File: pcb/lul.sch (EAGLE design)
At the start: 87 parts, among them IC1 STM32F072C8T6, IC2 REG1117, IC3 74AHCT1G08DBV, SW1 324_SW324_SWITCH_FOOT_HOLE, SW2 324_SW324_SWITCH_FOOT_HOLE, U1 UG-2864HSWEG01

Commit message: new buttons
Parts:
- removed S19, S20: TAC_SWITCHSMD, clock:TAC_SWITCHSMD
- removed U$12, U$13: M3_MOUNTING_HOLE, clock:M3_MOUNTING_HOLE
- added SW3, SW4: 6X6_SW, lul:6X6_SW
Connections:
- net BUTTON1: now also IC1PORTA_L.PA1, SW3.1; no longer IC1PORTB_H.PB12, S19.1, S19.2
- net BUTTON2: now also IC1PORTA_L.PA2, SW4.1; no longer IC1PORTB_H.PB11, S20.1, S20.2
- net GND: now also SW3.2, SW4.2; no longer S19.3, S19.4, S20.3, S20.4
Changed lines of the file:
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@@
 <part name="SD1" library="clock" deviceset="TF-HOLDER" device=""/>
 <part name="JP1" library="pinhead" library_urn="urn:adsk.eagle:library:325" deviceset="PINHD-1X5" device=""/>
-<part name="S19" library="clock" deviceset="TAC_SWITCH" device="SMD" value="TAC_SWITCHSMD"/>
-<part name="S20" library="clock" deviceset="TAC_SWITCH" device="SMD" value="TAC_SWITCHSMD"/>
 <part name="IC2" library="clock" deviceset="REG1117" device=""/>
 <part name="+3V3" library="supply1" library_urn="urn:adsk.eagle:library:371" deviceset="+3V3" device=""/>
@@
 <part name="U$10" library="clock" deviceset="M3_MOUNTING_HOLE" device=""/>
 <part name="U$11" library="clock" deviceset="M3_MOUNTING_HOLE" device=""/>
-<part name="U$12" library="clock" deviceset="M3_MOUNTING_HOLE" device=""/>
-<part name="U$13" library="clock" deviceset="M3_MOUNTING_HOLE" device=""/>
 <part name="U$14" library="clock" deviceset="M3_MOUNTING_HOLE" device=""/>
 <part name="U$15" library="clock" deviceset="M3_MOUNTING_HOLE" device=""/>
@@
 <part name="SW1" library="3pos_slide_switch" deviceset="324_SW" device="324_SWITCH_FOOT_HOLE" value="324_SW324_SWITCH_FOOT_HOLE"/>
 <part name="C28" library="clock" deviceset="CAP" device="0805" value="1uF"/>
+<part name="SW3" library="lul" deviceset="6X6_SW" device=""/>
+<part name="SW4" library="lul" deviceset="6X6_SW" device=""/>
 </parts>
 <sheets>
@@
 <instance part="SD1" gate="G$1" x="320.04" y="-162.56" rot="MR0"/>
 <instance part="JP1" gate="A" x="358.14" y="-193.04" rot="R180"/>
-<instance part="S19" gate="S" x="144.78" y="-170.18"/>
-<instance part="S20" gate="S" x="144.78" y="-193.04"/>
 <instance part="IC2" gate="G$1" x="109.22" y="-144.78"/>
 <instance part="+3V3" gate="G$1" x="353.06" y="76.2"/>
@@
 <instance part="+3V7" gate="G$1" x="259.08" y="-180.34" rot="MR0"/>
 <instance part="GND10" gate="1" x="254" y="-175.26"/>
-<instance part="GND11" gate="1" x="157.48" y="-175.26"/>
+<instance part="GND11" gate="1" x="172.72" y="-175.26"/>
 <instance part="+3V8" gate="G$1" x="294.64" y="-86.36"/>
 <instance part="GND12" gate="1" x="294.64" y="-121.92"/>
@@
 <instance part="R17" gate="G$1" x="408.94" y="-165.1" rot="R90"/>
 <instance part="GND45" gate="1" x="408.94" y="-175.26"/>
-<instance part="GND19" gate="1" x="154.94" y="-198.12"/>
+<instance part="GND19" gate="1" x="175.26" y="-198.12"/>
 <instance part="LED1" gate="G$1" x="-185.42" y="25.4" rot="MR0"/>
 <instance part="GND1" gate="1" x="139.7" y="-68.58"/>
@@
 <instance part="U$10" gate="G$1" x="467.36" y="33.02"/>
 <instance part="U$11" gate="G$1" x="523.24" y="33.02"/>
-<instance part="U$12" gate="G$1" x="523.24" y="15.24"/>
-<instance part="U$13" gate="G$1" x="495.3" y="33.02"/>
 <instance part="U$14" gate="G$1" x="467.36" y="15.24"/>
 <instance part="U$15" gate="G$1" x="495.3" y="48.26"/>
@@
 <instance part="SW1" gate="G$1" x="243.84" y="-205.74" rot="MR270"/>
 <instance part="C28" gate="G$1" x="335.28" y="-2.54" rot="R90"/>
+<instance part="SW3" gate="G$1" x="154.94" y="-172.72"/>
+<instance part="SW4" gate="G$1" x="152.4" y="-195.58"/>
 </instances>
 <busses>
@@
 <pinref part="U$3" gate="1" pin="GND"/>
 <junction x="297.18" y="-30.48"/>
-</segment>
-<segment>
-<pinref part="S19" gate="S" pin="4"/>
-<wire x1="149.86" y1="-172.72" x2="157.48" y2="-172.72" width="0.1524" layer="91"/>
-<pinref part="GND11" gate="1" pin="GND"/>
-<pinref part="S19" gate="S" pin="3"/>
-<wire x1="149.86" y1="-170.18" x2="149.86" y2="-172.72" width="0.1524" layer="91"/>
-<junction x="149.86" y="-172.72"/>
-</segment>
-<segment>
-<pinref part="S20" gate="S" pin="3"/>
-<pinref part="S20" gate="S" pin="4"/>
-<wire x1="149.86" y1="-193.04" x2="149.86" y2="-195.58" width="0.1524" layer="91"/>
-<pinref part="GND19" gate="1" pin="GND"/>
-<wire x1="149.86" y1="-195.58" x2="154.94" y2="-195.58" width="0.1524" layer="91"/>
-<junction x="149.86" y="-195.58"/>
 </segment>
 <segment>
@@
 <junction x="246.38" y="-172.72"/>
 </segment>
+<segment>
+<pinref part="GND11" gate="1" pin="GND"/>
+<pinref part="SW3" gate="G$1" pin="2"/>
+<wire x1="167.64" y1="-172.72" x2="172.72" y2="-172.72" width="0.1524" layer="91"/>
+</segment>
+<segment>
+<pinref part="GND19" gate="1" pin="GND"/>
+<pinref part="SW4" gate="G$1" pin="2"/>
+<wire x1="165.1" y1="-195.58" x2="175.26" y2="-195.58" width="0.1524" layer="91"/>
+</segment>
 </net>
 <net name="SCL" class="0">
@@
 <net name="BUTTON1" class="0">
 <segment>
-<pinref part="S19" gate="S" pin="2"/>
-<wire x1="127" y1="-172.72" x2="139.7" y2="-172.72" width="0.1524" layer="91"/>
-<pinref part="S19" gate="S" pin="1"/>
-<wire x1="139.7" y1="-170.18" x2="139.7" y2="-172.72" width="0.1524" layer="91"/>
-<junction x="139.7" y="-172.72"/>
+<wire x1="127" y1="-172.72" x2="142.24" y2="-172.72" width="0.1524" layer="91"/>
 <label x="127" y="-172.72" size="1.778" layer="95"/>
-</segment>
-<segment>
-<pinref part="IC1" gate="PORTB_H" pin="PB12"/>
-<wire x1="449.58" y1="-193.04" x2="434.34" y2="-193.04" width="0.1524" layer="91"/>
-<label x="439.42" y="-193.04" size="1.778" layer="95"/>
+<pinref part="SW3" gate="G$1" pin="1"/>
+</segment>
+<segment>
+<pinref part="IC1" gate="PORTA_L" pin="PA1"/>
+<wire x1="363.22" y1="-157.48" x2="391.16" y2="-157.48" width="0.1524" layer="91"/>
+<label x="365.76" y="-157.48" size="1.778" layer="95"/>
 </segment>
 </net>
 <net name="BUTTON2" class="0">
 <segment>
-<pinref part="S20" gate="S" pin="2"/>
 <wire x1="124.46" y1="-195.58" x2="139.7" y2="-195.58" width="0.1524" layer="91"/>
-<pinref part="S20" gate="S" pin="1"/>
-<wire x1="139.7" y1="-193.04" x2="139.7" y2="-195.58" width="0.1524" layer="91"/>
-<junction x="139.7" y="-195.58"/>
 <label x="124.46" y="-195.58" size="1.778" layer="95"/>
-</segment>
-<segment>
-<pinref part="IC1" gate="PORTB_H" pin="PB11"/>
-<wire x1="449.58" y1="-190.5" x2="434.34" y2="-190.5" width="0.1524" layer="91"/>
-<label x="439.42" y="-190.5" size="1.778" layer="95"/>
-</segment>
-</net>
+<pinref part="SW4" gate="G$1" pin="1"/>
+</segment>
+<segment>
+<pinref part="IC1" gate="PORTA_L" pin="PA2"/>
+<wire x1="363.22" y1="-160.02" x2="391.16" y2="-160.02" width="0.1524" layer="91"/>
+<label x="365.76" y="-160.02" size="1.778" layer="95"/>
+</segment>
+</net>

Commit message: clean up main folder
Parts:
- C1, C10, C11, C12, C13, C14, C15, C16, C17, C18, C19, C2, C20, C21, C22, C23, C24, C25, C9: value 0.1uF -> 100nF
- C8: value 2.2uF/16V -> 2.2uF
- R2, R4, R5: value 10k -> 10K
- R7, R8: value 4K7 -> 5.1K
- S1, S10, S11, S12, S13, S14, S15, S2, S3, S4, S5, S6, S7, S8, S9: value MOMENTARY-SWITCH-SPST-LED-PTH-CHERRY -> CHERRY-MX-LED; device lul:MOMENTARY-SWITCH-SPST-LED-PTH-CHERRY -> SparkFun-Cherry-MX-Switch-Breakout:CHERRY-MX-LED
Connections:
- net GND: now also S1.S2, S10.S2, S11.S2, S12.S2, S13.S2, S14.S2, S15.S2, S2.S2, S3.S2, S4.S2, S5.S2, S6.S2, S7.S2, S8.S2, S9.S2; no longer S1.2, S10.2, S11.2, S12.2, S13.2, S14.2, S15.2, S2.2, S3.2, S4.2, S5.2, S6.2, S7.2, S8.2, S9.2
- net SW1: now also S1.S1; no longer S1.1
- net SW10: now also S10.S1; no longer S10.1
- net SW11: now also S11.S1; no longer S11.1
- net SW12: now also S12.S1; no longer S12.1
- net SW13: now also S13.S1; no longer S13.1
- net SW14: now also S14.S1; no longer S14.1
- net SW15: now also S15.S1; no longer S15.1
- net SW2: now also S2.S1; no longer S2.1
- net SW3: now also S3.S1; no longer S3.1
- net SW4: now also S4.S1; no longer S4.1
- net SW5: now also S5.S1; no longer S5.1
- net SW6: now also S6.S1; no longer S6.1
- net SW7: now also S7.S1; no longer S7.1
- net SW8: now also S8.S1; no longer S8.1
- net SW9: now also S9.S1; no longer S9.1

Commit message: new pcb ready for fab
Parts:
- removed C26: 47uF, clock:C-USC1210
- added C29: 100nF, clock:CAP0805
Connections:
- net GND: now also C29.1; no longer C26.2
- net N$1: now also C29.2; no longer C26.1
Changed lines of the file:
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@@
 <part name="R1" library="joyAnalog" deviceset="RESISTOR" device="0805-RES" value="5.1K"/>
 <part name="R9" library="joyAnalog" deviceset="RESISTOR" device="0805-RES" value="5.1K"/>
-<part name="C26" library="clock" deviceset="C-US" device="C1210" value="47uF"/>
-<part name="GND5" library="supply1" library_urn="urn:adsk.eagle:library:371" deviceset="GND" device=""/>
 <part name="GND8" library="supply1" library_urn="urn:adsk.eagle:library:371" deviceset="GND" device=""/>
 <part name="SW2" library="3pos_slide_switch" deviceset="324_SW" device="324_SWITCH_FOOT_HOLE" value="324_SW324_SWITCH_FOOT_HOLE"/>
@@
 <part name="SW3" library="lul" deviceset="6X6_SW" device=""/>
 <part name="SW4" library="lul" deviceset="6X6_SW" device=""/>
+<part name="C29" library="clock" deviceset="CAP" device="0805" value="100nF"/>
+<part name="GND16" library="supply1" library_urn="urn:adsk.eagle:library:371" deviceset="GND" device=""/>
 </parts>
 <sheets>
@@
 <instance part="R1" gate="G$1" x="-5.08" y="-154.94" rot="MR0"/>
 <instance part="R9" gate="G$1" x="-5.08" y="-149.86" rot="MR0"/>
-<instance part="C26" gate="G$1" x="86.36" y="-147.32"/>
-<instance part="GND5" gate="1" x="86.36" y="-154.94"/>
 <instance part="GND8" gate="1" x="276.86" y="-213.36"/>
 <instance part="SW2" gate="G$1" x="241.3" y="-157.48" rot="MR90"/>
@@
 <instance part="SW3" gate="G$1" x="154.94" y="-172.72"/>
 <instance part="SW4" gate="G$1" x="152.4" y="-195.58"/>
+<instance part="C29" gate="G$1" x="78.74" y="-147.32" rot="R180"/>
+<instance part="GND16" gate="1" x="78.74" y="-154.94"/>
 </instances>
 <busses>
@@
 </segment>
 <segment>
-<pinref part="C26" gate="G$1" pin="2"/>
-<pinref part="GND5" gate="1" pin="GND"/>
-</segment>
-<segment>
 <pinref part="SW2" gate="G$1" pin="2"/>
 <pinref part="GND10" gate="1" pin="GND"/>
@@
 <pinref part="SW4" gate="G$1" pin="2"/>
 <wire x1="165.1" y1="-195.58" x2="175.26" y2="-195.58" width="0.1524" layer="91"/>
+</segment>
+<segment>
+<pinref part="C29" gate="G$1" pin="1"/>
+<pinref part="GND16" gate="1" pin="GND"/>
 </segment>
 </net>
@@
 <pinref part="U$8" gate="G$1" pin="VBUS"/>
 <pinref part="IC2" gate="G$1" pin="VIN"/>
-<wire x1="43.18" y1="-144.78" x2="86.36" y2="-144.78" width="0.1524" layer="91"/>
-<pinref part="C26" gate="G$1" pin="1"/>
-<wire x1="86.36" y1="-144.78" x2="96.52" y2="-144.78" width="0.1524" layer="91"/>
-<junction x="86.36" y="-144.78"/>
-</segment>
-</net>
+<wire x1="43.18" y1="-144.78" x2="78.74" y2="-144.78" width="0.1524" layer="91"/>
+<wire x1="78.74" y1="-144.78" x2="96.52" y2="-144.78" width="0.1524" layer="91"/>
+<pinref part="C29" gate="G$1" pin="2"/>
+<junction x="78.74" y="-144.78"/>
+</segment>
+</net>

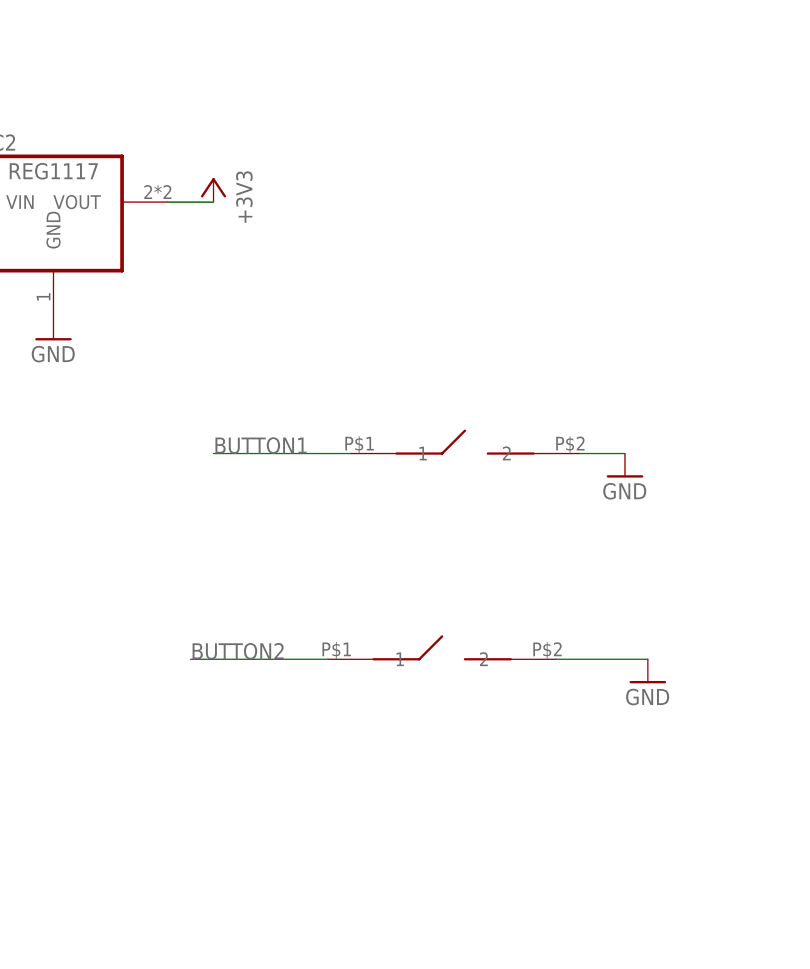
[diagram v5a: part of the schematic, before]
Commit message: firmware improvment, new plus/minus buttons
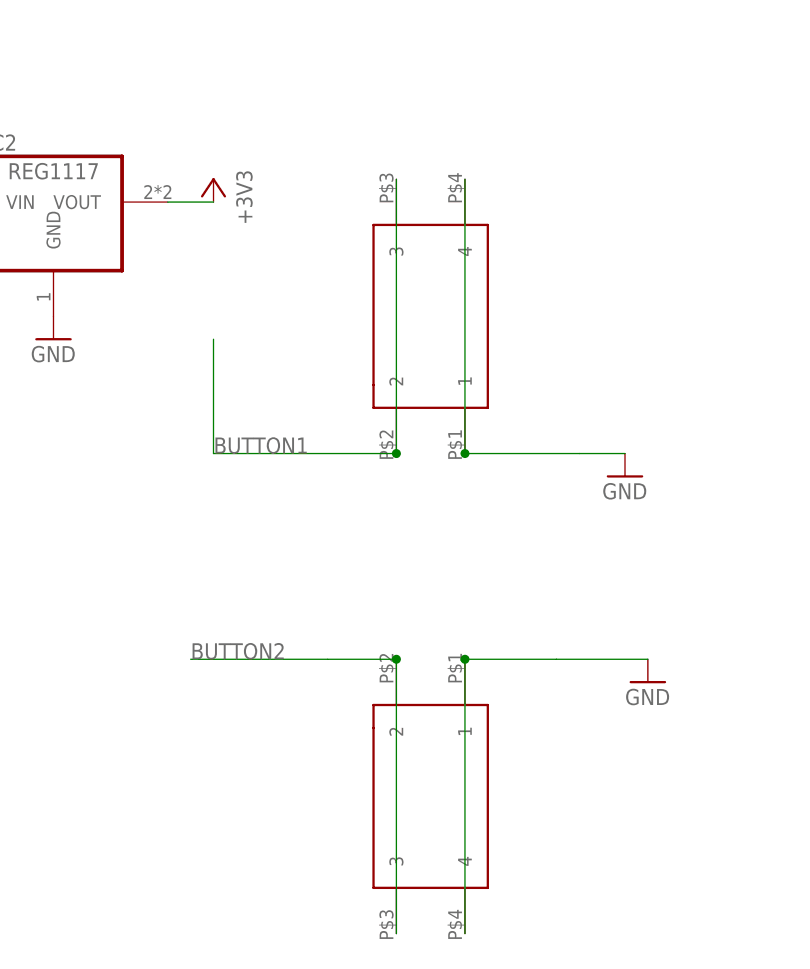
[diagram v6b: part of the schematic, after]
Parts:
- SW3, SW4: value 6X6_SW -> 324_SW324_SWITCH_FOOT_HOLE; device lul:6X6_SW -> 3pos_slide_switch:324_SW324_SWITCH_FOOT_HOLE
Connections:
- net BUTTON1: now also SW3.2, SW3.3; no longer SW3.1
- net BUTTON2: now also SW4.2, SW4.3; no longer SW4.1
- net GND: now also SW3.1, SW3.4, SW4.1, SW4.4; no longer SW3.2, SW4.2
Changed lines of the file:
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@@
 <part name="SW1" library="3pos_slide_switch" deviceset="324_SW" device="324_SWITCH_FOOT_HOLE" value="324_SW324_SWITCH_FOOT_HOLE"/>
 <part name="C28" library="clock" deviceset="CAP" device="0805" value="1uF"/>
-<part name="SW3" library="lul" deviceset="6X6_SW" device=""/>
-<part name="SW4" library="lul" deviceset="6X6_SW" device=""/>
 <part name="C29" library="clock" deviceset="CAP" device="0805" value="100nF"/>
 <part name="GND16" library="supply1" library_urn="urn:adsk.eagle:library:371" deviceset="GND" device=""/>
+<part name="SW3" library="3pos_slide_switch" deviceset="324_SW" device="324_SWITCH_FOOT_HOLE" value="324_SW324_SWITCH_FOOT_HOLE"/>
+<part name="SW4" library="3pos_slide_switch" deviceset="324_SW" device="324_SWITCH_FOOT_HOLE" value="324_SW324_SWITCH_FOOT_HOLE"/>
 </parts>
 <sheets>
@@
 <instance part="SW1" gate="G$1" x="243.84" y="-205.74" rot="MR270"/>
 <instance part="C28" gate="G$1" x="335.28" y="-2.54" rot="R90"/>
-<instance part="SW3" gate="G$1" x="154.94" y="-172.72"/>
-<instance part="SW4" gate="G$1" x="152.4" y="-195.58"/>
 <instance part="C29" gate="G$1" x="78.74" y="-147.32" rot="R180"/>
 <instance part="GND16" gate="1" x="78.74" y="-154.94"/>
+<instance part="SW3" gate="G$1" x="152.4" y="-157.48" rot="R90"/>
+<instance part="SW4" gate="G$1" x="152.4" y="-210.82" rot="MR270"/>
 </instances>
 <busses>
@@
 <segment>
 <pinref part="GND11" gate="1" pin="GND"/>
-<pinref part="SW3" gate="G$1" pin="2"/>
 <wire x1="167.64" y1="-172.72" x2="172.72" y2="-172.72" width="0.1524" layer="91"/>
+<pinref part="SW3" gate="G$1" pin="1"/>
+<wire x1="154.94" y1="-172.72" x2="167.64" y2="-172.72" width="0.1524" layer="91"/>
+<pinref part="SW3" gate="G$1" pin="4"/>
+<wire x1="154.94" y1="-142.24" x2="154.94" y2="-172.72" width="0.1524" layer="91"/>
+<junction x="154.94" y="-172.72"/>
 </segment>
 <segment>
 <pinref part="GND19" gate="1" pin="GND"/>
-<pinref part="SW4" gate="G$1" pin="2"/>
 <wire x1="165.1" y1="-195.58" x2="175.26" y2="-195.58" width="0.1524" layer="91"/>
+<pinref part="SW4" gate="G$1" pin="1"/>
+<wire x1="154.94" y1="-195.58" x2="165.1" y2="-195.58" width="0.1524" layer="91"/>
+<pinref part="SW4" gate="G$1" pin="4"/>
+<wire x1="154.94" y1="-195.58" x2="154.94" y2="-226.06" width="0.1524" layer="91"/>
+<junction x="154.94" y="-195.58"/>
 </segment>
 <segment>
@@
 <net name="BUTTON1" class="0">
 <segment>
-<wire x1="127" y1="-172.72" x2="142.24" y2="-172.72" width="0.1524" layer="91"/>
 <label x="127" y="-172.72" size="1.778" layer="95"/>
-<pinref part="SW3" gate="G$1" pin="1"/>
+<wire x1="127" y1="-160.02" x2="127" y2="-172.72" width="0.1524" layer="91"/>
+<pinref part="SW3" gate="G$1" pin="2"/>
+<wire x1="127" y1="-172.72" x2="147.32" y2="-172.72" width="0.1524" layer="91"/>
+<pinref part="SW3" gate="G$1" pin="3"/>
+<wire x1="147.32" y1="-142.24" x2="147.32" y2="-172.72" width="0.1524" layer="91"/>
+<junction x="147.32" y="-172.72"/>
 </segment>
 <segment>
@@
 <wire x1="124.46" y1="-195.58" x2="139.7" y2="-195.58" width="0.1524" layer="91"/>
 <label x="124.46" y="-195.58" size="1.778" layer="95"/>
-<pinref part="SW4" gate="G$1" pin="1"/>
-</segment>
-<segment>
+<pinref part="SW4" gate="G$1" pin="2"/>
+<wire x1="139.7" y1="-195.58" x2="147.32" y2="-195.58" width="0.1524" layer="91"/>
+<pinref part="SW4" gate="G$1" pin="3"/>
+<wire x1="147.32" y1="-195.58" x2="147.32" y2="-226.06" width="0.1524" layer="91"/>
+<junction x="147.32" y="-195.58"/>
+</segment>
+<segment>

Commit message: production run 1
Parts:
- renumbered U$8 to U2
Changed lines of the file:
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@@
 <part name="IC3" library="74xx-little-de" library_urn="urn:adsk.eagle:library:86" deviceset="74*1G08" device="DBV" technology="AHCT"/>
 <part name="GND31" library="supply1" library_urn="urn:adsk.eagle:library:371" deviceset="GND" device=""/>
-<part name="U$8" library="my_usbc_16p" deviceset="USBC_16P" device=""/>
+<part name="U2" library="my_usbc_16p" deviceset="USBC_16P" device=""/>
 <part name="GND6" library="supply1" deviceset="GND" device=""/>
 <part name="R1" library="joyAnalog" deviceset="RESISTOR" device="0805-RES" value="5.1K"/>
@@
 <instance part="IC3" gate="P" x="-63.5" y="50.8"/>
 <instance part="GND31" gate="1" x="-45.72" y="7.62"/>
-<instance part="U$8" gate="G$1" x="27.94" y="-165.1" rot="MR0"/>
+<instance part="U2" gate="G$1" x="27.94" y="-165.1" rot="MR0"/>
 <instance part="GND6" gate="1" x="-10.16" y="-172.72" rot="MR0"/>
 <instance part="R1" gate="G$1" x="-5.08" y="-154.94" rot="MR0"/>
@@
 <pinref part="R9" gate="G$1" pin="2"/>
 <wire x1="-10.16" y1="-149.86" x2="-10.16" y2="-154.94" width="0.1524" layer="91"/>
-<pinref part="U$8" gate="G$1" pin="GND"/>
+<pinref part="U2" gate="G$1" pin="GND"/>
 <wire x1="43.18" y1="-165.1" x2="-10.16" y2="-165.1" width="0.1524" layer="91"/>
 <junction x="-10.16" y="-165.1"/>
@@
 <wire x1="58.42" y1="-149.86" x2="45.72" y2="-149.86" width="0.1524" layer="91"/>
 <label x="60.96" y="-149.86" size="1.778" layer="95"/>
-<pinref part="U$8" gate="G$1" pin="DP1"/>
+<pinref part="U2" gate="G$1" pin="DP1"/>
 <wire x1="45.72" y1="-149.86" x2="43.18" y2="-149.86" width="0.1524" layer="91"/>
 <wire x1="45.72" y1="-149.86" x2="45.72" y2="-152.4" width="0.1524" layer="91"/>
 <junction x="45.72" y="-149.86"/>
-<pinref part="U$8" gate="G$1" pin="DP2"/>
+<pinref part="U2" gate="G$1" pin="DP2"/>
 <wire x1="45.72" y1="-152.4" x2="43.18" y2="-152.4" width="0.1524" layer="91"/>
 </segment>
@@
 <wire x1="10.16" y1="-152.4" x2="2.54" y2="-152.4" width="0.1524" layer="91"/>
 <wire x1="2.54" y1="-152.4" x2="2.54" y2="-154.94" width="0.1524" layer="91"/>
-<pinref part="U$8" gate="G$1" pin="CC2"/>
+<pinref part="U2" gate="G$1" pin="CC2"/>
 </segment>
 </net>
@@
 <pinref part="R9" gate="G$1" pin="1"/>
 <wire x1="10.16" y1="-149.86" x2="0" y2="-149.86" width="0.1524" layer="91"/>
-<pinref part="U$8" gate="G$1" pin="CC1"/>
+<pinref part="U2" gate="G$1" pin="CC1"/>
 </segment>
 </net>
 <net name="N$1" class="0">
 <segment>
-<pinref part="U$8" gate="G$1" pin="VBUS"/>
+<pinref part="U2" gate="G$1" pin="VBUS"/>
 <pinref part="IC2" gate="G$1" pin="VIN"/>
 <wire x1="43.18" y1="-144.78" x2="78.74" y2="-144.78" width="0.1524" layer="91"/>
@@
 <segment>
 <wire x1="58.42" y1="-157.48" x2="45.72" y2="-157.48" width="0.1524" layer="91"/>
-<pinref part="U$8" gate="G$1" pin="DN1"/>
+<pinref part="U2" gate="G$1" pin="DN1"/>
 <wire x1="45.72" y1="-157.48" x2="43.18" y2="-157.48" width="0.1524" layer="91"/>
 <label x="60.96" y="-157.48" size="1.778" layer="95"/>
-<pinref part="U$8" gate="G$1" pin="DN2"/>
+<pinref part="U2" gate="G$1" pin="DN2"/>
 <wire x1="43.18" y1="-160.02" x2="45.72" y2="-160.02" width="0.1524" layer="91"/>
 <wire x1="45.72" y1="-160.02" x2="45.72" y2="-157.48" width="0.1524" layer="91"/>
